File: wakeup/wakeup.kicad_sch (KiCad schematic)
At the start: 15 parts, among them J1 Conn_01x03_Female, U1 74HC00, U2 74HC393

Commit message: non function changes
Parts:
- D1: value D -> 1n4148
- J1: value Conn_01x03_Female -> Connector
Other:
- moved on the sheet: D1, J1, U1B
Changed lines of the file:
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@@
   (junction (at 135.89 68.58) (diameter 0) (color 0 0 0 0)
   )
-  (junction (at 146.05 87.63) (diameter 0) (color 0 0 0 0)
+  (junction (at 144.78 87.63) (diameter 0) (color 0 0 0 0)
   )
   (junction (at 101.6 90.17) (diameter 0) (color 0 0 0 0)
@@
     (stroke (width 0) (type default) (color 0 0 0 0))
   )
-  (wire (pts (xy 158.75 92.71) (xy 158.75 90.17))
+  (wire (pts (xy 157.48 92.71) (xy 157.48 90.17))
     (stroke (width 0) (type default) (color 0 0 0 0))
   )
@@
     (stroke (width 0) (type default) (color 0 0 0 0))
   )
-  (wire (pts (xy 146.05 87.63) (xy 148.59 87.63))
+  (wire (pts (xy 144.78 87.63) (xy 147.32 87.63))
     (stroke (width 0) (type default) (color 0 0 0 0))
   )
@@
     (stroke (width 0) (type default) (color 0 0 0 0))
   )
-  (wire (pts (xy 158.75 82.55) (xy 158.75 85.09))
+  (wire (pts (xy 157.48 82.55) (xy 157.48 85.09))
     (stroke (width 0) (type default) (color 0 0 0 0))
   )
@@
     (stroke (width 0) (type default) (color 0 0 0 0))
   )
-  (wire (pts (xy 158.75 85.09) (xy 161.29 85.09))
+  (wire (pts (xy 157.48 85.09) (xy 160.02 85.09))
     (stroke (width 0) (type default) (color 0 0 0 0))
   )
@@
     (stroke (width 0) (type default) (color 0 0 0 0))
   )
-  (wire (pts (xy 146.05 93.98) (xy 129.54 93.98))
+  (wire (pts (xy 144.78 93.98) (xy 129.54 93.98))
     (stroke (width 0) (type default) (color 0 0 0 0))
   )
@@
     (stroke (width 0) (type default) (color 0 0 0 0))
   )
-  (wire (pts (xy 156.21 87.63) (xy 161.29 87.63))
+  (wire (pts (xy 154.94 87.63) (xy 160.02 87.63))
     (stroke (width 0) (type default) (color 0 0 0 0))
   )
@@
     (stroke (width 0) (type default) (color 0 0 0 0))
   )
-  (wire (pts (xy 146.05 87.63) (xy 146.05 93.98))
+  (wire (pts (xy 144.78 87.63) (xy 144.78 93.98))
     (stroke (width 0) (type default) (color 0 0 0 0))
   )
@@
     (stroke (width 0) (type default) (color 0 0 0 0))
   )
-  (wire (pts (xy 143.51 87.63) (xy 146.05 87.63))
+  (wire (pts (xy 142.24 87.63) (xy 144.78 87.63))
     (stroke (width 0) (type default) (color 0 0 0 0))
   )
@@
     (stroke (width 0) (type default) (color 0 0 0 0))
   )
-  (wire (pts (xy 158.75 90.17) (xy 161.29 90.17))
+  (wire (pts (xy 157.48 90.17) (xy 160.02 90.17))
     (stroke (width 0) (type default) (color 0 0 0 0))
   )
@@
     (stroke (width 0) (type default) (color 0 0 0 0))
   )
-  (wire (pts (xy 123.19 88.9) (xy 133.35 88.9))
+  (wire (pts (xy 123.19 88.9) (xy 132.08 88.9))
     (stroke (width 0) (type default) (color 0 0 0 0))
   )
@@
     (stroke (width 0) (type default) (color 0 0 0 0))
   )
-  (wire (pts (xy 123.19 86.36) (xy 133.35 86.36))
+  (wire (pts (xy 123.19 86.36) (xy 132.08 86.36))
     (stroke (width 0) (type default) (color 0 0 0 0))
   )
@@
     (pin "2")
   )
-  (symbol (lib_id "power:GND") (at 158.75 92.71 0) (unit 1)
-    (in_bom yes) (on_board yes) (fields_autoplaced)
-    (property "Reference" "#PWR07" (id 0) (at 158.75 99.06 0)
-      (effects (font (size 1.27 1.27)) hide)
-    )
-    (property "Value" "GND" (id 1) (at 158.75 97.79 0))
-    (property "Footprint" "" (id 2) (at 158.75 92.71 0)
-      (effects (font (size 1.27 1.27)) hide)
-    )
-    (property "Datasheet" "" (id 3) (at 158.75 92.71 0)
+  (symbol (lib_id "power:GND") (at 157.48 92.71 0) (unit 1)
+    (in_bom yes) (on_board yes) (fields_autoplaced)
+    (property "Reference" "#PWR07" (id 0) (at 157.48 99.06 0)
+      (effects (font (size 1.27 1.27)) hide)
+    )
+    (property "Value" "GND" (id 1) (at 157.48 97.79 0))
+    (property "Footprint" "" (id 2) (at 157.48 92.71 0)
+      (effects (font (size 1.27 1.27)) hide)
+    )
+    (property "Datasheet" "" (id 3) (at 157.48 92.71 0)
       (effects (font (size 1.27 1.27)) hide)
     )
@@
     (pin "13")
   )
-  (symbol (lib_id "74IEC:74HC00") (at 138.43 87.63 0) (unit 2)
-    (in_bom yes) (on_board yes)
-    (property "Reference" "U1" (id 0) (at 138.43 83.82 0))
-    (property "Value" "74HC00" (id 1) (at 138.43 91.44 0))
-    (property "Footprint" "Package_SO:SO-14_3.9x8.65mm_P1.27mm" (id 2) (at 138.43 93.98 0)
-      (effects (font (size 1.27 1.27)) hide)
-    )
-    (property "Datasheet" "https://www.ti.com/lit/ds/symlink/sn7400.pdf" (id 3) (at 138.43 83.82 0)
+  (symbol (lib_id "74IEC:74HC00") (at 137.16 87.63 0) (unit 2)
+    (in_bom yes) (on_board yes)
+    (property "Reference" "U1" (id 0) (at 137.16 83.82 0))
+    (property "Value" "74HC00" (id 1) (at 137.16 91.44 0))
+    (property "Footprint" "Package_SO:SO-14_3.9x8.65mm_P1.27mm" (id 2) (at 137.16 93.98 0)
+      (effects (font (size 1.27 1.27)) hide)
+    )
+    (property "Datasheet" "https://www.ti.com/lit/ds/symlink/sn7400.pdf" (id 3) (at 137.16 83.82 0)
       (effects (font (size 1.27 1.27)) hide)
     )
@@
     (pin "2")
   )
-  (symbol (lib_id "Device:D") (at 152.4 87.63 0) (unit 1)
-    (in_bom yes) (on_board yes) (fields_autoplaced)
-    (property "Reference" "D1" (id 0) (at 152.4 81.28 0))
-    (property "Value" "D" (id 1) (at 152.4 83.82 0))
-    (property "Footprint" "" (id 2) (at 152.4 87.63 0)
-      (effects (font (size 1.27 1.27)) hide)
-    )
-    (property "Datasheet" "~" (id 3) (at 152.4 87.63 0)
+  (symbol (lib_id "Device:D") (at 151.13 87.63 0) (unit 1)
+    (in_bom yes) (on_board yes)
+    (property "Reference" "D1" (id 0) (at 151.13 83.82 0))
+    (property "Value" "1n4148" (id 1) (at 151.13 91.44 0))
+    (property "Footprint" "" (id 2) (at 151.13 87.63 0)
+      (effects (font (size 1.27 1.27)) hide)
+    )
+    (property "Datasheet" "~" (id 3) (at 151.13 87.63 0)
       (effects (font (size 1.27 1.27)) hide)
     )
@@
     (pin "9")
   )
-  (symbol (lib_id "power:VCC") (at 158.75 82.55 0) (unit 1)
-    (in_bom yes) (on_board yes) (fields_autoplaced)
-    (property "Reference" "#PWR05" (id 0) (at 158.75 86.36 0)
-      (effects (font (size 1.27 1.27)) hide)
-    )
-    (property "Value" "VCC" (id 1) (at 158.75 77.47 0))
-    (property "Footprint" "" (id 2) (at 158.75 82.55 0)
-      (effects (font (size 1.27 1.27)) hide)
-    )
-    (property "Datasheet" "" (id 3) (at 158.75 82.55 0)
+  (symbol (lib_id "power:VCC") (at 157.48 82.55 0) (unit 1)
+    (in_bom yes) (on_board yes) (fields_autoplaced)
+    (property "Reference" "#PWR05" (id 0) (at 157.48 86.36 0)
+      (effects (font (size 1.27 1.27)) hide)
+    )
+    (property "Value" "VCC" (id 1) (at 157.48 77.47 0))
+    (property "Footprint" "" (id 2) (at 157.48 82.55 0)
+      (effects (font (size 1.27 1.27)) hide)
+    )
+    (property "Datasheet" "" (id 3) (at 157.48 82.55 0)
       (effects (font (size 1.27 1.27)) hide)
     )
@@
     (pin "13")
   )
-  (symbol (lib_id "Connector:Conn_01x03_Female") (at 166.37 87.63 0) (unit 1)
-    (in_bom yes) (on_board yes) (fields_autoplaced)
-    (property "Reference" "J1" (id 0) (at 167.64 86.3599 0)
-      (effects (font (size 1.27 1.27)) (justify left))
-    )
-    (property "Value" "Conn_01x03_Female" (id 1) (at 167.64 88.8999 0)
-      (effects (font (size 1.27 1.27)) (justify left))
-    )
-    (property "Footprint" "Connector_PinSocket_2.54mm:PinSocket_1x03_P2.54mm_Vertical" (id 2) (at 166.37 87.63 0)
-      (effects (font (size 1.27 1.27)) hide)
-    )
-    (property "Datasheet" "~" (id 3) (at 166.37 87.63 0)
+  (symbol (lib_id "Connector:Conn_01x03_Female") (at 165.1 87.63 0) (unit 1)
+    (in_bom yes) (on_board yes)
+    (property "Reference" "J1" (id 0) (at 165.1 82.55 0))
+    (property "Value" "Connector" (id 1) (at 165.1 92.71 0))
+    (property "Footprint" "Connector_PinSocket_2.54mm:PinSocket_1x03_P2.54mm_Vertical" (id 2) (at 165.1 87.63 0)
+      (effects (font (size 1.27 1.27)) hide)
+    )
+    (property "Datasheet" "~" (id 3) (at 165.1 87.63 0)
       (effects (font (size 1.27 1.27)) hide)
     )
@@
     )
     (path "/73e9b2dc-e516-489c-bad5-4d0f9f05c72b"
-      (reference "D1") (unit 1) (value "D") (footprint "")
+      (reference "D1") (unit 1) (value "1n4148") (footprint "")
     )
     (path "/c0ac4adc-1766-46e3-9139-a9cacdb1fe63"
-      (reference "J1") (unit 1) (value "Conn_01x03_Female") (footprint "Connector_PinSocket_2.54mm:PinSocket_1x03_P2.54mm_Vertical")
+      (reference "J1") (unit 1) (value "Connector") (footprint "Connector_PinSocket_2.54mm:PinSocket_1x03_P2.54mm_Vertical")
     )
     (path "/a71539b7-6be1-48ce-a90f-d231122870e8"

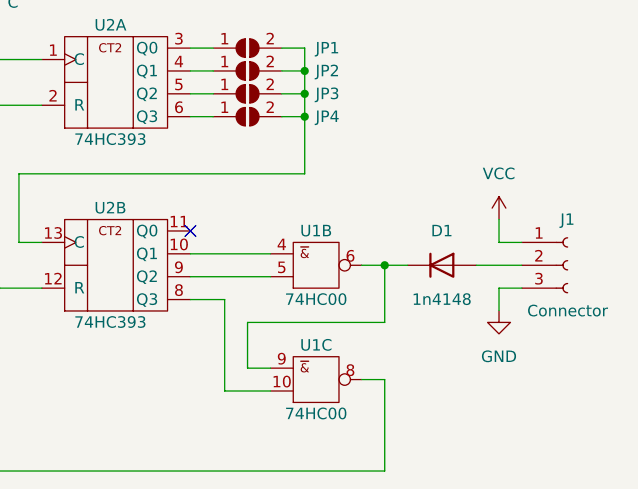
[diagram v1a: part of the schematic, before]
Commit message: fix 74IEC library Add stlink connector info delete unused picture update symbols for ZX-Spectrum-Pentagon
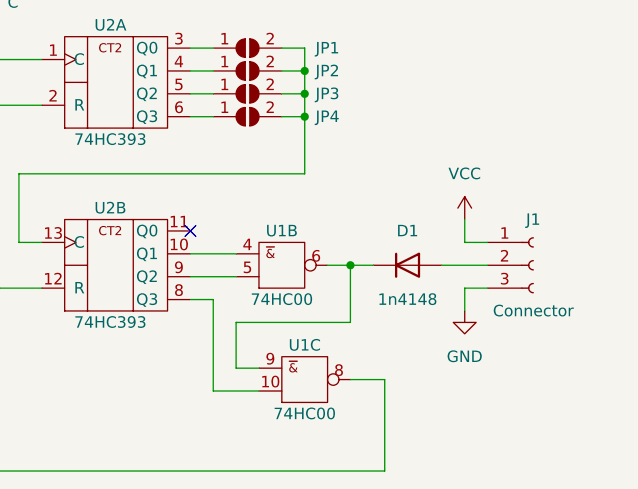
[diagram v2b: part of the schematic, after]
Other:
- moved on the sheet: D1, J1, U1B, U1C

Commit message: non functional update
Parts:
- added U? (x2): 74HC74, symbol 74IEC:74HC74
- added U?: 74HC86, symbol 74IEC:74HC86
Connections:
- net GND: now also U?.7 (GND), U?.7 (GND), U?.7 (GND)
- net VCC: now also U?.1 (~{R}), U?.10 (~{S}), U?.13 (~{R}), U?.14 (VCC), U?.14 (VCC), U?.14 (VCC), U?.4 (~{S})
- new net: U?.12 (D), U?.5 (Q)
- new net: U?.2 (B), U?.9 (Q)
- new net DD23::1::3: U?.1 (A)
- new net GOUT: U?.3 (Y)
- new net MOSI: U?.2 (D)
- new net PIXCLK: U?.11 (C)
- new net SCK: U?.3 (C)
